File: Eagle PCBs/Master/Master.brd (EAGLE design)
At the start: 79.7 x 36.8 mm, 15 parts

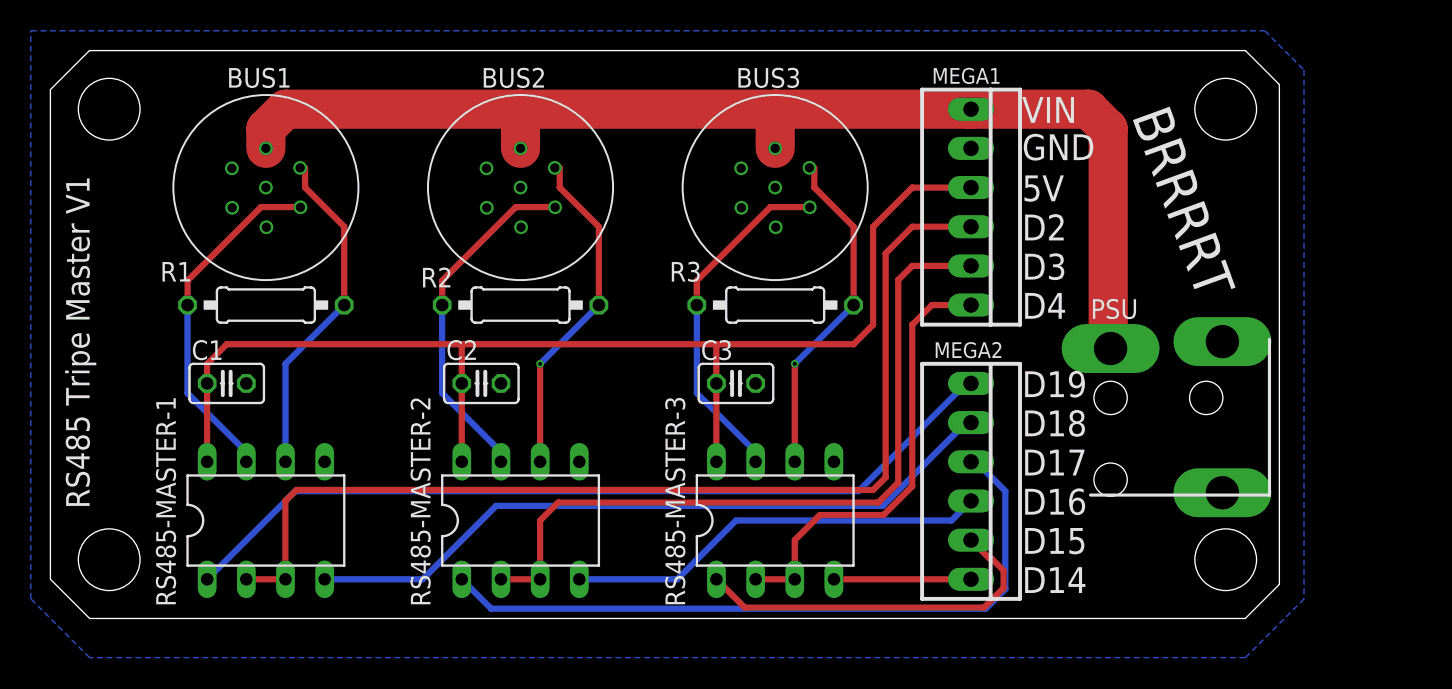
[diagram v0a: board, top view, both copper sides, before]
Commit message: Updated GX12 footprint and finalized first revison of Master PCB
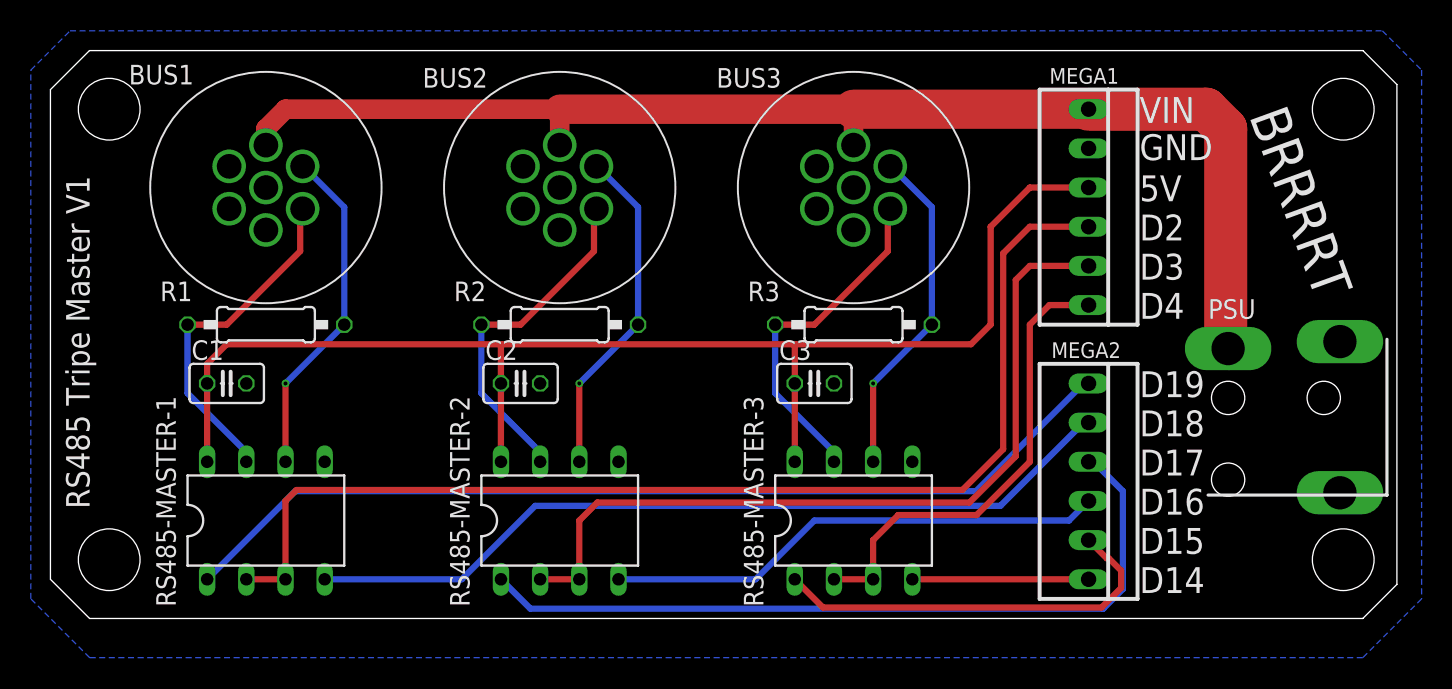
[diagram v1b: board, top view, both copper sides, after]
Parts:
- moved MEGA1 7.62 mm to (67.3, 26.7)
- moved MEGA2 7.62 mm to (67.3, 8.89)
- moved PSU 7.62 mm to (80.1, 13.1)
- moved R3 5.24 mm to (52.1, 19.1)
- moved BUS3 5.08 mm to (52.1, 27.9)
- moved C3 5.08 mm to (49.5, 15.2)
- moved RS485-MASTER-3 5.08 mm to (52.1, 6.35)
- moved R2 2.84 mm to (33.0, 19.1)
- moved BUS2 2.54 mm to (33.0, 27.9)
- moved RS485-MASTER-2 2.54 mm to (33.0, 6.35)
- moved C2 2.54 mm to (30.5, 15.2)
- moved R1 1.27 mm to (14.0, 19.1)
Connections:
- net GND: now also BUS1.6, BUS2.6, BUS3.6; no longer BUS1.7, BUS2.7, BUS3.7
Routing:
- net MEGA_D19: track 54.8 -> 62.4 mm
- net MEGA_D18: track 46.1 -> 53.7 mm
- net 5VCC: track 79.6 -> 87.2 mm
- net VCC: track 76.3 -> 83.3 mm
- net MEGA_D2: track 67.9 -> 74.5 mm
- net MEGA_D16: track 27.5 -> 32.6 mm
- net MEGA_D17: track 45.9 -> 51.0 mm
- net MEGA_D3: track 48.8 -> 52.9 mm
- net MEGA_D15: track 24.0 -> 26.5 mm
- net MEGA_D14: track 8.89 -> 11.4 mm
- net MEGA_D4: track 29.0 -> 30.6 mm
- net RS485_1_A: track 22.0 -> 21.9 mm, vias 0 -> 1
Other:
- board size 79.7 x 36.8 mm -> 87.3 x 36.8 mm

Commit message: New slave PCB
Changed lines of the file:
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@@
 <setting verticaltext="up"/>
 </settings>
-<grid distance="50" unitdist="mil" unit="mil" style="lines" multiple="1" display="no" altdistance="5" altunitdist="mil" altunit="mil"/>
+<grid distance="50" unitdist="mil" unit="mm" style="lines" multiple="1" display="no" altdistance="5" altunitdist="mil" altunit="mil"/>
 <layers>
 <layer number="1" name="Top" color="4" fill="1" visible="yes" active="yes"/>
@@
 <wire x1="85.1" y1="36.82" x2="2.53" y2="36.82" width="0" layer="20"/>
 <wire x1="2.53" y1="36.82" x2="0" y2="34.29" width="0" layer="20"/>
-<hole x="3.81" y="33.02" drill="4"/>
-<hole x="3.81" y="3.81" drill="4"/>
-<hole x="83.82" y="33.02" drill="4"/>
-<hole x="83.82" y="3.81" drill="4"/>
+<hole x="3.81" y="33.02" drill="3.5"/>
+<hole x="3.81" y="3.81" drill="3.5"/>
+<hole x="83.82" y="33.02" drill="3.5"/>
+<hole x="83.82" y="3.81" drill="3.5"/>
 <text x="70.612" y="32.131" size="1.6764" layer="25">VIN</text>
 <text x="70.612" y="29.718" size="1.6764" layer="25">GND</text>
